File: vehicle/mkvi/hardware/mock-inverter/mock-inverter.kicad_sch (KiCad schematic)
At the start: 64 parts, among them J1 MicroFit_RA_4, J2 TagConnect_6, J3 MicroFit_RA_3, K1 3350-4275, U1 MAX7221CWG_1, U2 ATMEGA16M1, U3 TLV76780DBVR, U4 MCP2561-E_SN, U5 ADUM4150ARIZ-RL, U6 ADS7816U, Y1 Crystal_SMD

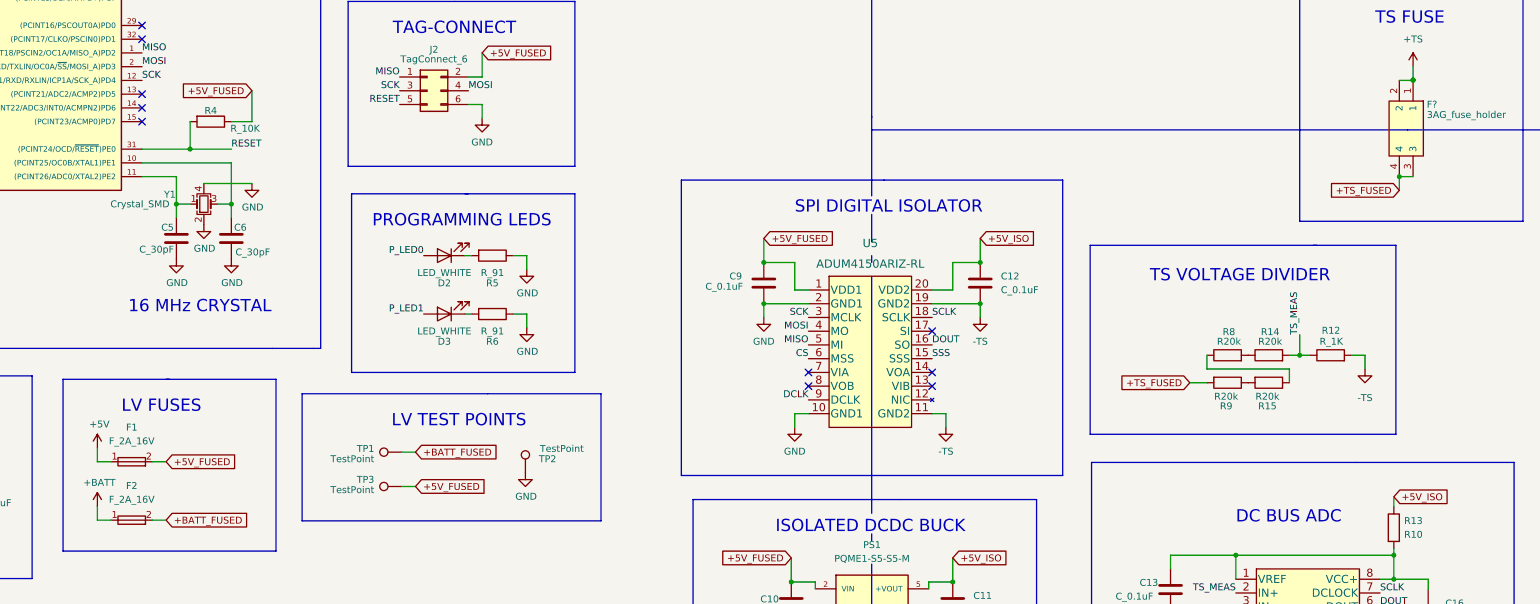
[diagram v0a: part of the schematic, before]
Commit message: Fix tag connect symbol
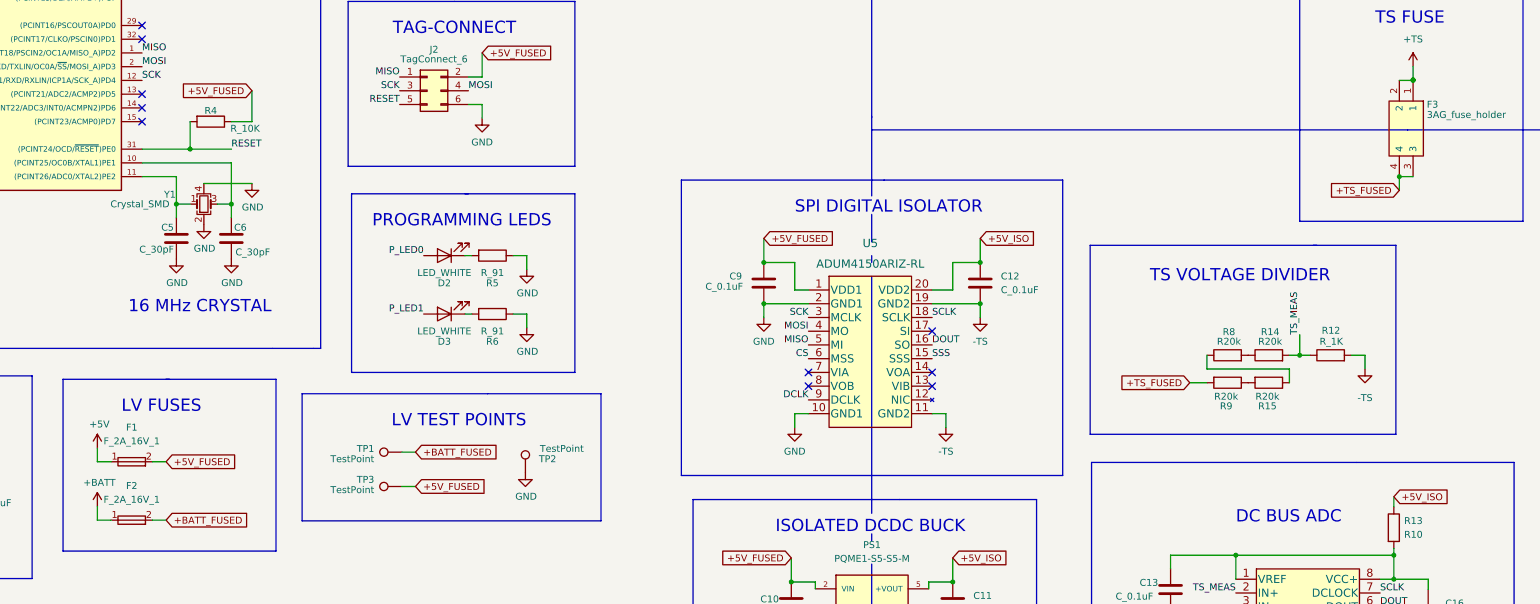
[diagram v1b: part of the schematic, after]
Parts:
- removed F1, F2: F_2A_16V, footprints:Fuse_1812_4532Metric, symbol formula:F_2A_16V
- added F1, F2: F_2A_16V_1, footprints:Fuse_1812_4532Metric, symbol formula:F_2A_16V_1
- gave numbers to parts that had none: 1
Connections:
- net +5V: now also F1.1
- net +5V_FUSED: now also F1.2
- net +BATT: now also F2.1
- net +BATT_FUSED: now also F2.2
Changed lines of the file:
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@@
     (pin "1")
+  )
+  (symbol (lib_id "formula:F_2A_16V_1") (at 98.425 168.91 0) (unit 1)
+    (in_bom yes) (on_board yes) (fields_autoplaced)
+    (property "Reference" "F2" (id 0) (at 98.425 162.56 0))
+    (property "Value" "F_2A_16V_1" (id 1) (at 98.425 165.1 0))
+    (property "Footprint" "footprints:Fuse_1812_4532Metric" (id 2) (at 98.425 160.02 0)
+      (effects (font (size 1.27 1.27)) hide)
+    )
+    (property "Datasheet" "https://www.belfuse.com/resources/datasheets/circuitprotection/ds-cp-0zcg-series.pdf" (id 3) (at 97.79 153.035 0)
+      (effects (font (size 1.27 1.27)) hide)
+    )
+    (property "PurchasingLink" "https://www.digikey.com/en/products/detail/bel-fuse-inc/0ZCG0200AF2B/6210545" (id 4) (at 95.25 156.845 0)
+      (effects (font (size 1.27 1.27)) hide)
+    )
+    (property "MPN" "0ZCG0200AF2B" (id 5) (at 98.425 163.195 0)
+      (effects (font (size 1.27 1.27)) hide)
+    )
+    (pin "1")
+    (pin "2")
   )
   (symbol (lib_id "power:GND") (at 149.86 54.61 0) (unit 1)
@@
   (symbol (lib_id "formula:3AG_fuse_holder_1") (at 335.28 86.36 270) (unit 1)
     (in_bom yes) (on_board yes)
-    (property "Reference" "F?" (id 0) (at 337.82 92.075 90)
+    (property "Reference" "F3" (id 0) (at 337.82 92.075 90)
       (effects (font (size 1.27 1.27)) (justify left))
     )
@@
     (pin "1")
   )
+  (symbol (lib_id "formula:F_2A_16V_1") (at 98.425 158.115 0) (unit 1)
+    (in_bom yes) (on_board yes) (fields_autoplaced)
+    (property "Reference" "F1" (id 0) (at 98.425 151.765 0))
+    (property "Value" "F_2A_16V_1" (id 1) (at 98.425 154.305 0))
+    (property "Footprint" "footprints:Fuse_1812_4532Metric" (id 2) (at 98.425 149.225 0)
+      (effects (font (size 1.27 1.27)) hide)
+    )
+    (property "Datasheet" "https://www.belfuse.com/resources/datasheets/circuitprotection/ds-cp-0zcg-series.pdf" (id 3) (at 97.79 142.24 0)
+      (effects (font (size 1.27 1.27)) hide)
+    )
+    (property "PurchasingLink" "https://www.digikey.com/en/products/detail/bel-fuse-inc/0ZCG0200AF2B/6210545" (id 4) (at 95.25 146.05 0)
+      (effects (font (size 1.27 1.27)) hide)
+    )
+    (property "MPN" "0ZCG0200AF2B" (id 5) (at 98.425 152.4 0)
+      (effects (font (size 1.27 1.27)) hide)
+    )
+    (pin "1")
+    (pin "2")
+  )
   (symbol (lib_id "power:GND") (at 171.196 160.147 0) (unit 1)
     (in_bom yes) (on_board yes)
@@
     (pin "9")
   )
-  (symbol (lib_name "F_2A_16V_1") (lib_id "formula:F_2A_16V") (at 98.425 158.115 0) (unit 1)
-    (in_bom yes) (on_board yes) (fields_autoplaced)
-    (property "Reference" "F1" (id 0) (at 98.425 151.765 0))
-    (property "Value" "F_2A_16V" (id 1) (at 98.425 154.305 0))
-    (property "Footprint" "footprints:Fuse_1812_4532Metric" (id 2) (at 98.425 149.225 0)
-      (effects (font (size 1.27 1.27)) hide)
-    )
-    (property "Datasheet" "https://www.belfuse.com/resources/datasheets/circuitprotection/ds-cp-0zcg-series.pdf" (id 3) (at 97.79 142.24 0)
-      (effects (font (size 1.27 1.27)) hide)
-    )
-    (property "PurchasingLink" "https://www.digikey.com/en/products/detail/bel-fuse-inc/0ZCG0200AF2B/6210545" (id 4) (at 95.25 146.05 0)
-      (effects (font (size 1.27 1.27)) hide)
-    )
-    (property "MPN" "0ZCG0200AF2B" (id 5) (at 98.425 152.4 0)
-      (effects (font (size 1.27 1.27)) hide)
-    )
-    (pin "1")
-    (pin "2")
-  )
   (symbol (lib_id "formula:-TS") (at 299.974 189.992 0) (unit 1)
     (in_bom yes) (on_board yes) (fields_autoplaced)
@@
     (pin "3")
   )
-  (symbol (lib_name "F_2A_16V_1") (lib_id "formula:F_2A_16V") (at 98.425 168.91 0) (unit 1)
-    (in_bom yes) (on_board yes) (fields_autoplaced)
-    (property "Reference" "F2" (id 0) (at 98.425 162.56 0))
-    (property "Value" "F_2A_16V" (id 1) (at 98.425 165.1 0))
-    (property "Footprint" "footprints:Fuse_1812_4532Metric" (id 2) (at 98.425 160.02 0)
-      (effects (font (size 1.27 1.27)) hide)
-    )
-    (property "Datasheet" "https://www.belfuse.com/resources/datasheets/circuitprotection/ds-cp-0zcg-series.pdf" (id 3) (at 97.79 153.035 0)
-      (effects (font (size 1.27 1.27)) hide)
-    )
-    (property "PurchasingLink" "https://www.digikey.com/en/products/detail/bel-fuse-inc/0ZCG0200AF2B/6210545" (id 4) (at 95.25 156.845 0)
-      (effects (font (size 1.27 1.27)) hide)
-    )
-    (property "MPN" "0ZCG0200AF2B" (id 5) (at 98.425 163.195 0)
-      (effects (font (size 1.27 1.27)) hide)
-    )
-    (pin "1")
-    (pin "2")
-  )
   (symbol (lib_id "power:GND") (at 36.83 46.99 0) (unit 1)
     (in_bom yes) (on_board yes)
@@
       (reference "D7") (unit 1) (value "LED_WHITE") (footprint "footprints:LED_0805_OEM")
     )
-    (path "/e7a1f7c5-ac72-4c91-ac37-848a95383cb5"
-      (reference "F1") (unit 1) (value "F_2A_16V") (footprint "footprints:Fuse_1812_4532Metric")
-    )
-    (path "/f8d46ebd-718e-48b9-a735-33223a8ff5a1"
-      (reference "F2") (unit 1) (value "F_2A_16V") (footprint "footprints:Fuse_1812_4532Metric")
+    (path "/9c170fb3-a04b-4e18-aa86-f75ed55c80b5"
+      (reference "F1") (unit 1) (value "F_2A_16V_1") (footprint "footprints:Fuse_1812_4532Metric")
+    )
+    (path "/25308d5a-2e12-4526-bacc-a6b9e0b16949"
+      (reference "F2") (unit 1) (value "F_2A_16V_1") (footprint "footprints:Fuse_1812_4532Metric")
     )
     (path "/8fe491a3-0f0f-4aaf-acc8-6292887f8cc5"
-      (reference "F?") (unit 1) (value "3AG_fuse_holder") (footprint "footprints:4245")
+      (reference "F3") (unit 1) (value "3AG_fuse_holder") (footprint "footprints:4245")
     )
     (path "/cc76d178-27f2-4db1-9851-5d5d347a01cd"
